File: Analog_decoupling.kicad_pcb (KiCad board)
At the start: 2 copper layers, 188.1 x 142 mm, 118 parts, among them J1 22-23-2021, J2 22-23-2021, J3 22-23-2021, J4 302-S101, J5 OSTTC020162, U1 LT1129CST-5#PBF, U10 TLV9001IDBVR, U11 TLV9001IDBVR, U2 ISO224ADWVR, U3 TLV9001IDBVR, U4 TLV9001IDBVR, U5 ISO224ADWVR, U6 TLV9001IDBVR, U7 TLV9001IDBVR, U8 REF1933AIDDCT, U9 ISO224ADWVR

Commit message: OA pinout corrected. Mounting holes deleted
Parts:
- removed the REF** at (198.9, 111.6)
- removed the REF** at (247.5, 188.8)
- removed the REF** at (247.5, 55.8)
- removed the REF** at (147.3, 111.5)
- removed the REF** at (96.4, 111.5)
- removed the REF** at (69.3, 169.9)
- removed the REF** at (116.6, 168.3)
- removed the REF** at (247.0, 166.1)
- removed the REF** at (247.0, 179.1)
- removed the REF** at (67.5, 55.8)
- removed the REF** at (67.5, 188.8)
- added REF**: ESD-Logo_8.9x8mm_SilkScreen, Symbol:ESD-Logo_8.9x8mm_SilkScreen, F.Cu at (111.5, 186.0)
- PS3: value (none) -> TMH2415S
- R1, R10, R15, R16, R2, R21, R24, R29, R30, R35, R38, R7: footprint Resistor_SMD:R_0603_1608Metric_Pad0.98x0.95mm_HandSolder -> Resistor_SMD:R_0603_1608Metric
- R11, R12, R13, R14, R18, R19, R20, R22, R23, R25, R26, R27, R28, R32, R33, R34, R36, R37, R39, R4, R40, R41, R42, R5, R6, R8, R9: footprint Resistor_SMD:R_0805_2012Metric_Pad1.20x1.40mm_HandSolder -> Resistor_SMD:R_0805_2012Metric
- U10, U11, U3, U4, U6, U7: footprint Package_TO_SOT_SMD:SOT-23-5_HandSoldering -> Package_TO_SOT_SMD:SOT-23-5
- moved C10 8.86 mm to (144.1, 116.8)
- moved C19 8.47 mm to (195.4, 117.0)
- moved C1 8.31 mm to (92.9, 116.9)
- moved C6 1.13 mm to (212.5, 142.2), turned to 270 degrees
- moved U10 0.89 mm to (202.8, 131.1), turned to 180 degrees
- moved U6 0.79 mm to (151.1, 131.0), turned to 180 degrees
- moved U4 0.77 mm to (87.2, 128.5), turned to 90 degrees
- moved U7 0.59 mm to (138.5, 128.5), turned to 90 degrees
- moved U11 0.56 mm to (190.3, 128.6), turned to 90 degrees
- moved U3 0.43 mm to (99.6, 131.4), turned to 180 degrees
- moved R10 0.41 mm to (95.9, 131.3)
- moved R1 0.40 mm to (103.3, 131.3)
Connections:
- U10 pad 1: Net-(R29-Pad1) -> Net-(R33-Pad1)
- U10 pad 3: Net-(R34-Pad1) -> Net-(R29-Pad1)
- U10 pad 4: Net-(R33-Pad1) -> Net-(R34-Pad1)
- U11 pad 1: Net-(R39-Pad1) -> Net-(R40-Pad1)
- U11 pad 3: Net-(R36-Pad1) -> Net-(R39-Pad1)
- U11 pad 4: Net-(R40-Pad1) -> Net-(R36-Pad1)
- U3 pad 1: Net-(R1-Pad1) -> Net-(R5-Pad1)
- U3 pad 3: Net-(R10-Pad1) -> Net-(R1-Pad1)
- U3 pad 4: Net-(R5-Pad1) -> Net-(R10-Pad1)
- U4 pad 1: Net-(R11-Pad1) -> Net-(R12-Pad1)
- U4 pad 3: Net-(R8-Pad1) -> Net-(R11-Pad1)
- U4 pad 4: Net-(R12-Pad1) -> Net-(R8-Pad1)
- U6 pad 1: Net-(R15-Pad1) -> Net-(R19-Pad1)
- U6 pad 3: Net-(R20-Pad1) -> Net-(R15-Pad1)
- U6 pad 4: Net-(R19-Pad1) -> Net-(R20-Pad1)
- U7 pad 1: Net-(R25-Pad1) -> Net-(R26-Pad1)
- U7 pad 3: Net-(R22-Pad1) -> Net-(R25-Pad1)
- U7 pad 4: Net-(R26-Pad1) -> Net-(R22-Pad1)
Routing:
- net GNDREF: track 546.0 -> 457.2 mm, vias 41 -> 215
- net +5V_Analog: track 330.9 -> 355.0 mm, vias 16 -> 20
- net Net-(R26-Pad1): track 39.6 -> 19.5 mm
- net Net-(R40-Pad1): track 36.7 -> 17.6 mm
- net +24V: track 199.4 -> 193.9 mm
- net Net-(R33-Pad1): track 8.49 -> 11.9 mm
- net Net-(R19-Pad1): track 8.69 -> 12.0 mm
- net Net-(R5-Pad1): track 9.11 -> 11.0 mm
- net Net-(R20-Pad1): track 14.2 -> 13.5 mm
- net Net-(R8-Pad1): track 6.79 -> 7.43 mm
- net Net-(R10-Pad1): track 13.6 -> 13.0 mm
- net Net-(R1-Pad1): track 16.8 -> 16.2 mm
- net Net-(R12-Pad1): track 19.7 -> 19.2 mm
- net (no net): vias 0 -> 8
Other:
- board text added: "+24V"
- board text added: "ADC1_P"
- board text added: "ADC2_P"
- board text added: "ADC3_P"
- board text added: "A_CH1_FAULT"
- board text added: "A_CH2 _FAULT"
- board text added: "A_CH3_FAULT"
- board text added: "GND"
- board text added: "PCB ver. 1.1"
- board text added: "ЦМН"

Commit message: All mistakes corrected
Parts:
- added REF**: MountingHole_2.1mm, MountingHole:MountingHole_2.1mm, F.Cu at (194.4, 111.5)
- added REF**: MountingHole_2.1mm, MountingHole:MountingHole_2.1mm, F.Cu at (142.6, 111.5)
- added REF**: MountingHole_2.1mm, MountingHole:MountingHole_2.1mm, F.Cu at (92.2, 111.5)
- added REF**: MountingHole_3.7mm_Pad, MountingHole:MountingHole_3.7mm_Pad, F.Cu at (247.5, 56.3)
- added REF**: MountingHole_3.7mm_Pad, MountingHole:MountingHole_3.7mm_Pad, F.Cu at (247.5, 188.3)
- added REF**: MountingHole_3.7mm_Pad, MountingHole:MountingHole_3.7mm_Pad, F.Cu at (67.5, 188.3)
- added REF**: MountingHole_3.7mm_Pad, MountingHole:MountingHole_3.7mm_Pad, F.Cu at (67.5, 56.3)
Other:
- board text added: "High voltage area"

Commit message: Analog decoupling PCB converted to KiCAD6 format and pass DRC
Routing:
- net Net-(C3-Pad2): track 64.4 -> 63.8 mm
- net (no net): vias 8 -> 0
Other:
- net class Default removed
- net class Power removed

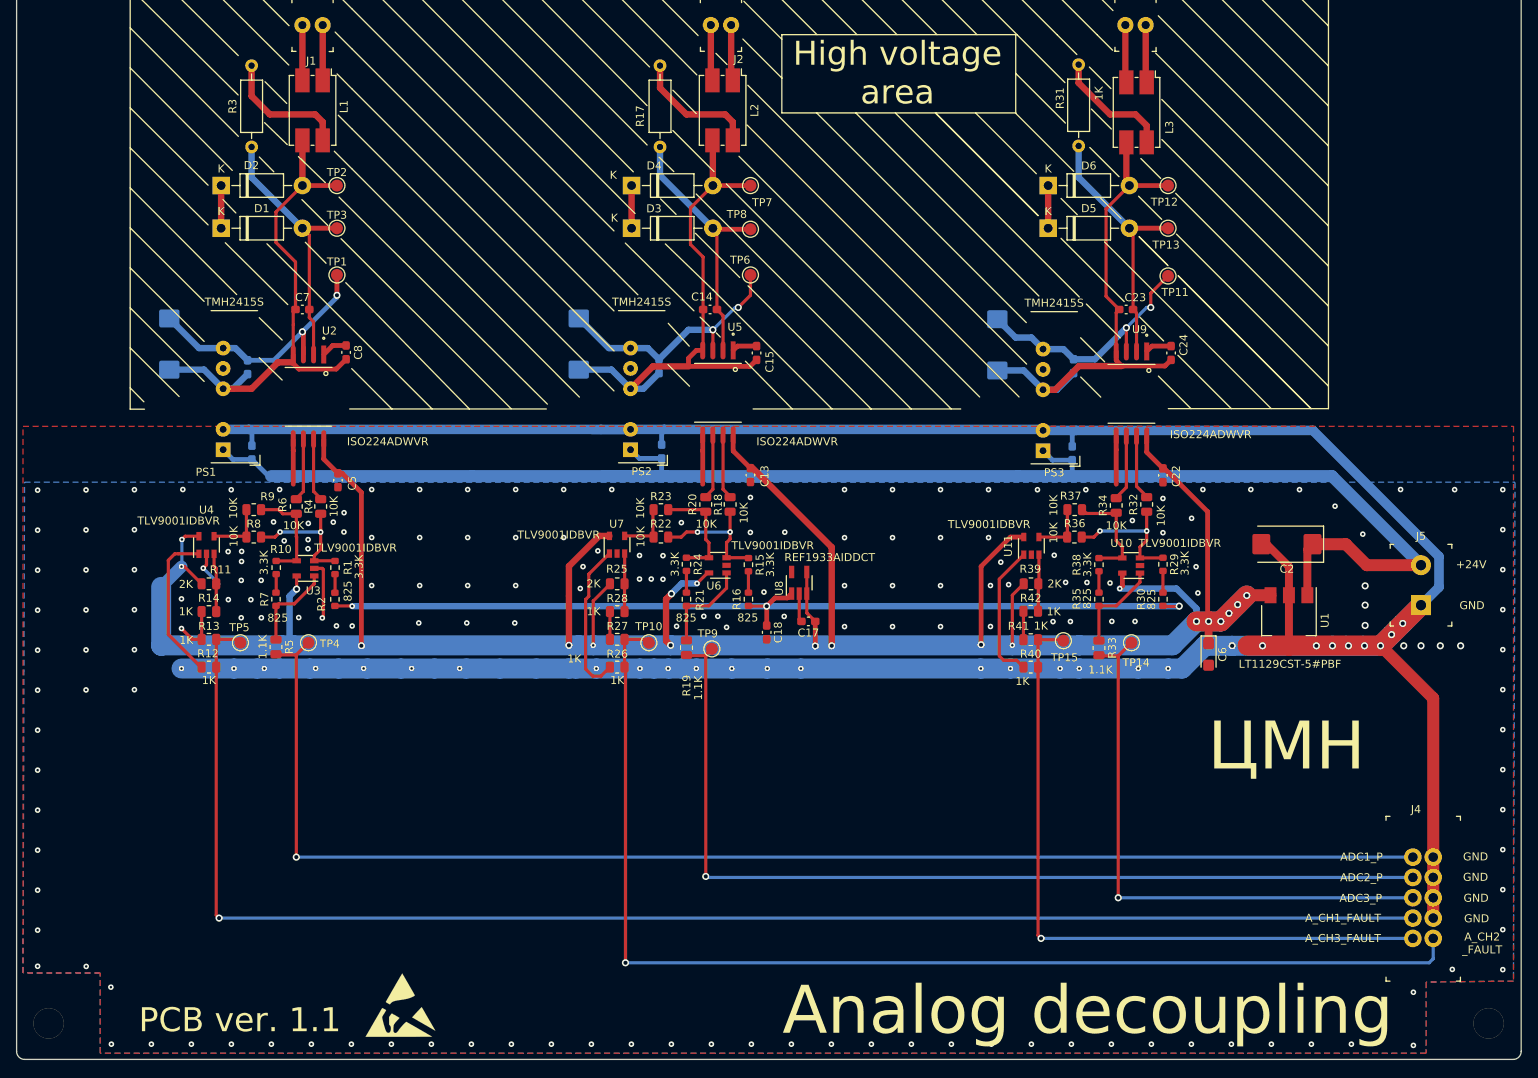
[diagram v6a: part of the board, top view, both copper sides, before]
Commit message: Analog decoupling PCB added LDOs for ISO224, added power LEDs
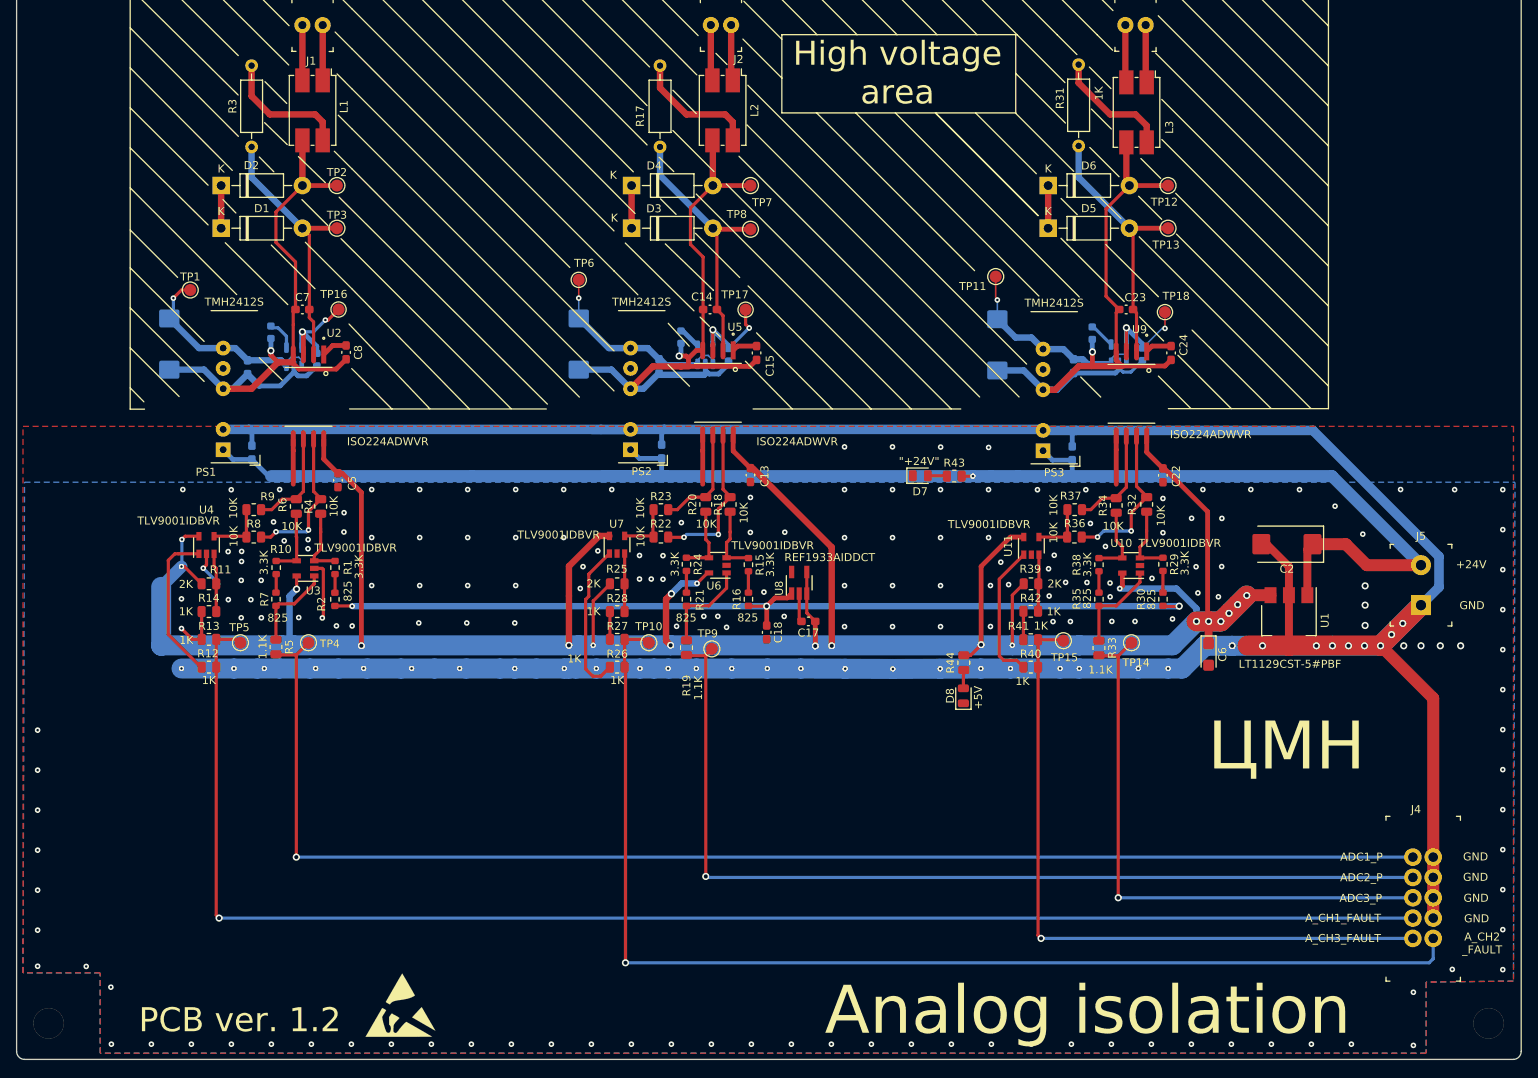
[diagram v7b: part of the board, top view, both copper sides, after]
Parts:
- added C16: 2.2µF, Capacitor_SMD:C_0603_1608Metric, B.Cu at (101.0, 105.3)
- added C25: 0.01µF, Capacitor_SMD:C_0603_1608Metric, B.Cu at (146.5, 102.5)
- added C26: 2.2µF, Capacitor_SMD:C_0603_1608Metric, B.Cu at (152.5, 104.7)
- added C27: 0.01µF, Capacitor_SMD:C_0603_1608Metric, B.Cu at (197.9, 102.0)
- added C28: 2.2µF, Capacitor_SMD:C_0603_1608Metric, B.Cu at (204.2, 104.7)
- added C9: 0.01µF, Capacitor_SMD:C_0603_1608Metric, B.Cu at (95.2, 101.9)
- added D7: FYLS-0805BUGC, LED_SMD:LED_0805_2012Metric, F.Cu at (176.4, 119.8)
- added D8: FYLS-0805BUGC, LED_SMD:LED_0805_2012Metric, F.Cu at (181.8, 147.3)
- added R43: 1.1K, Resistor_SMD:R_0805_2012Metric, F.Cu at (180.7, 119.9)
- added R44: 150, Resistor_SMD:R_0805_2012Metric, F.Cu at (181.9, 143.2)
- added TP16: TestPoint, TestPoint:TestPoint_Pad_D1.5mm, F.Cu at (103.7, 99.1)
- added TP17: TestPoint, TestPoint:TestPoint_Pad_D1.5mm, F.Cu at (154.6, 99.1)
- added TP18: TestPoint, TestPoint:TestPoint_Pad_D1.5mm, F.Cu at (207.0, 99.4)
- added U12: LP2985A-50DBVR, Package_TO_SOT_SMD:SOT-23-5, B.Cu at (98.1, 105.0)
- added U13: LP2985A-50DBVR, Package_TO_SOT_SMD:SOT-23-5, B.Cu at (149.5, 104.7)
- added U14: LP2985A-50DBVR, Package_TO_SOT_SMD:SOT-23-5, B.Cu at (201.2, 104.6)
- PS1, PS2, PS3: value TMH2415S -> TMH2412S
- moved TP11 21.5 mm to (185.9, 94.9)
- moved TP6 21.5 mm to (133.7, 95.4)
- moved TP1 18.4 mm to (85.2, 96.6)
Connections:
- PS1 pad 5: Net-(PS1-Pad5) -> unconnected-(PS1-Pad5)
- PS2 pad 5: Net-(PS2-Pad5) -> unconnected-(PS2-Pad5)
- PS3 pad 5: Net-(PS3-Pad5) -> unconnected-(PS3-Pad5)
- R22 pad 2: Net-(R15-Pad1) -> Net-(R18-Pad2)
- R23 pad 2: Net-(R20-Pad1) -> Net-(R20-Pad2)
- R36 pad 2: Net-(R29-Pad1) -> Net-(R32-Pad2)
- R37 pad 2: Net-(R34-Pad1) -> Net-(R34-Pad2)
- R8 pad 2: Net-(R1-Pad1) -> Net-(R4-Pad2)
- R9 pad 2: Net-(R10-Pad1) -> Net-(R6-Pad2)
- U2 pad 3: Net-(C3-Pad1) -> Net-(C16-Pad1)
- U5 pad 3: Net-(C11-Pad1) -> Net-(C26-Pad1)
- U8 pad 5: Net-(U8-Pad5) -> unconnected-(U8-Pad5)
- U9 pad 3: Net-(C20-Pad1) -> Net-(C28-Pad1)
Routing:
- net Net-(C16-Pad2): track 63.8 -> 78.7 mm, vias 0 -> 1
- net Net-(C20-Pad2): track 64.2 -> 78.8 mm, vias 0 -> 1
- net Net-(C28-Pad1): track 0.00 -> 14.3 mm, vias 0 -> 2
- net Net-(C16-Pad1): track 0.00 -> 14.1 mm, vias 0 -> 2
- net Net-(C11-Pad2): track 65.1 -> 79.0 mm, vias 0 -> 1
- net Net-(C26-Pad1): track 0.00 -> 13.9 mm, vias 0 -> 2
- net Net-(R18-Pad2): track 8.02 -> 19.7 mm, vias 0 -> 2
- net Net-(R32-Pad2): track 8.05 -> 19.6 mm, vias 0 -> 2
- net Net-(R4-Pad2): track 7.77 -> 18.5 mm, vias 0 -> 2
- net Net-(R29-Pad1): track 17.3 -> 8.92 mm, vias 2 -> 0
- net Net-(R15-Pad1): track 16.5 -> 8.60 mm, vias 2 -> 0
- net Net-(R1-Pad1): track 16.2 -> 8.73 mm, vias 2 -> 0
- net Net-(C20-Pad1): track 31.7 -> 24.9 mm, vias 2 -> 1
- net Net-(C11-Pad1): track 32.0 -> 25.5 mm, vias 2 -> 1
- net Net-(C3-Pad1): track 32.1 -> 25.8 mm, vias 2 -> 1
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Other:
- board text added: "+5V"
- board text added: "Analog isolation"
- board text added: "PCB ver. 1.2"
- board text added: "{dblquote}+24V{dblquote}"
- board text removed: "Analog decoupling"
- board text removed: "PCB ver. 1.1"

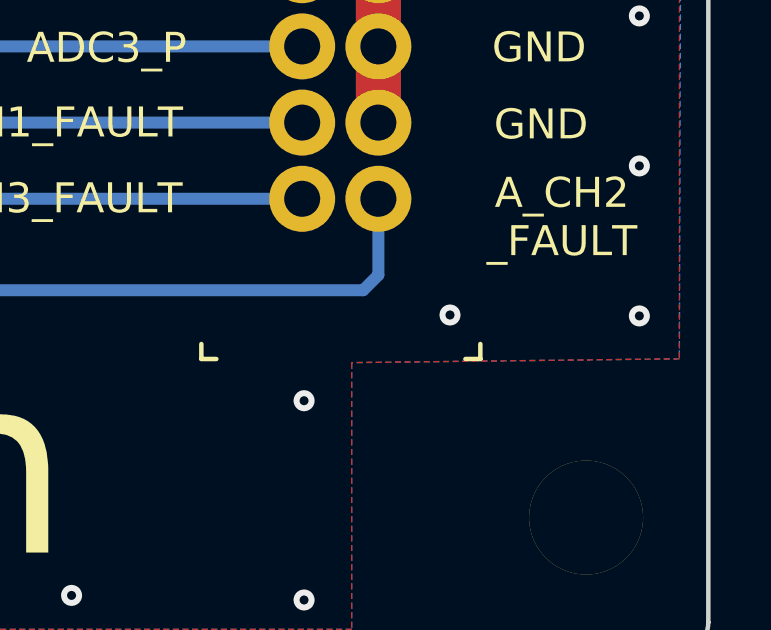
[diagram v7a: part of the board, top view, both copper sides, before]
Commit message: Analog decoupling PCB added LDOs for ISO224, added power LEDs
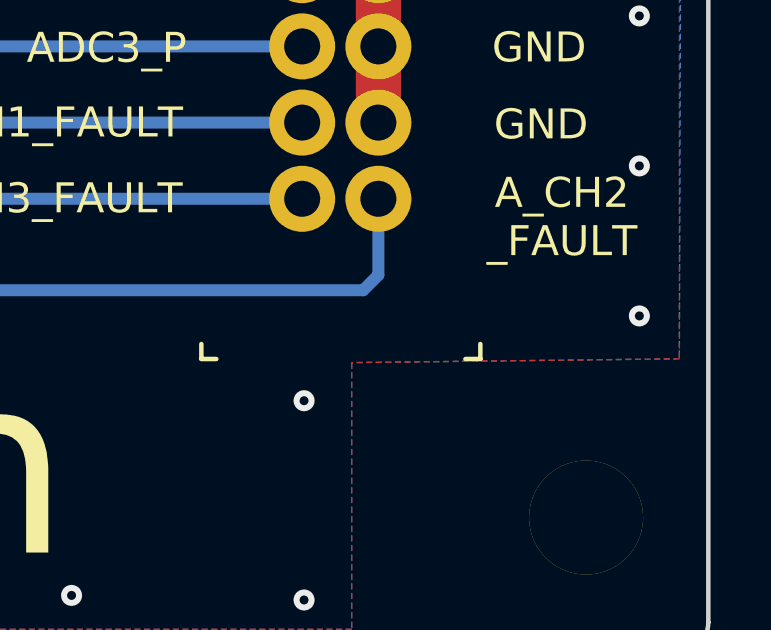
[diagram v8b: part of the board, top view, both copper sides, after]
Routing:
- net GNDREF: vias 213 -> 212
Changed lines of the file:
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@@
   (via (at 192.4558 131.4704) (size 0.7) (drill 0.3) (layers "F.Cu" "B.Cu") (free) (net 1))
   (via (at 207.9498 137.7442) (size 0.7) (drill 0.3) (layers "F.Cu" "B.Cu") (free) (net 1))
-  (via (at 242.9256 181.5465) (size 0.7) (drill 0.3) (layers "F.Cu" "B.Cu") (net 1))
   (via (at 197.2564 133.1849) (size 0.7) (drill 0.3) (layers "F.Cu" "B.Cu") (net 1))
   (via (at 152.860989 143.938011) (size 0.7) (drill 0.3) (layers "F.Cu" "B.Cu") (net 1))
